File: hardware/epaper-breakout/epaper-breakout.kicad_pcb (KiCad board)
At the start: 2 copper layers, 100 x 40.5 mm, 88 parts, among them J1 XF2M-3315-1A, J2 C10418, J3 Conn_02x06_Counter_Clockwise, J4 ED060SC4, J5 Conn_01x02_Male, Q1 AO3401A, Q2 AO3401A, Q3 MMBT3904, Q4 MMBT3904, Q5 AO3401A, Q6 MMBT3904, U1 MCP1700-3302E_SOT23, U10 ED060SC7, U11 TP4056, U12 CH340C, U2 LT1945, U3 LT1945, U4 XC6206PxxxMR, U5 ESP32-WROVER, U6 ED060XC5, U7 LM358, U8 74HC4094-normal, U9 MCP9700AT-ETT

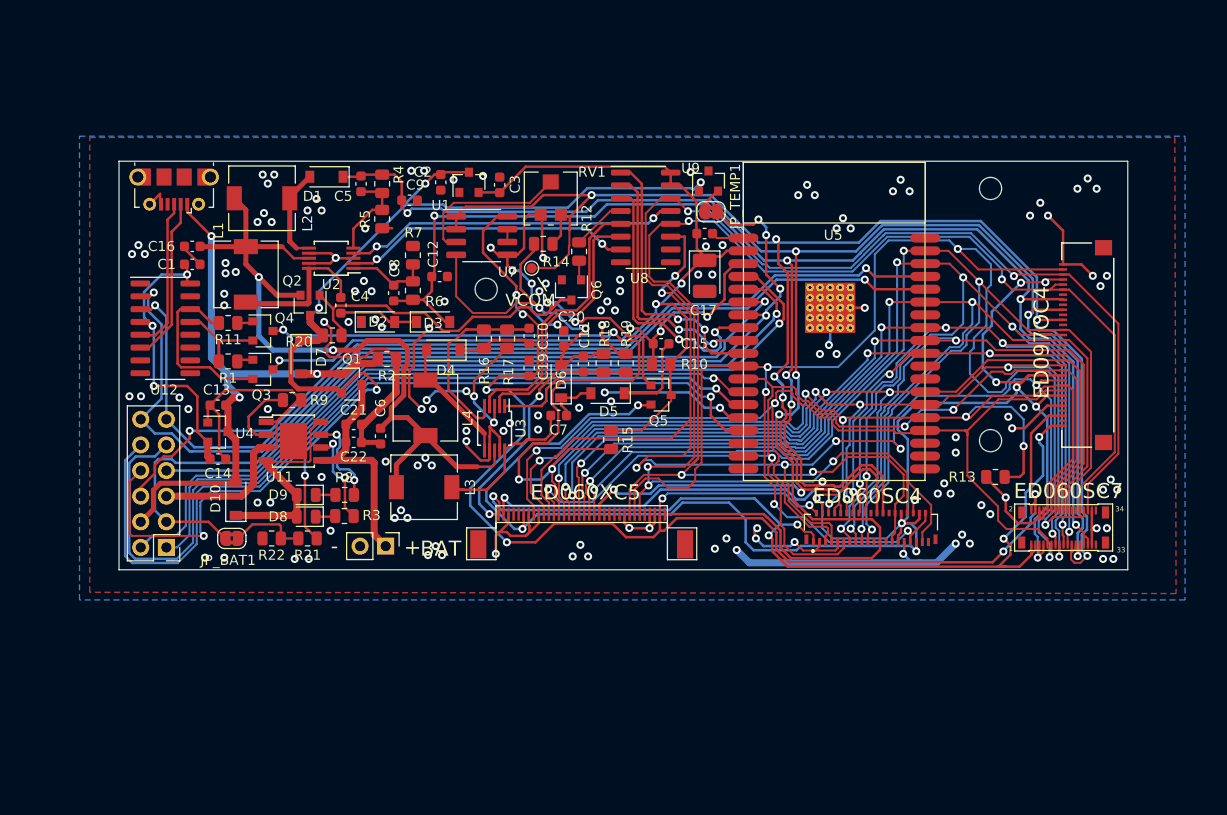
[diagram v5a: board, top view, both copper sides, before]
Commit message: add decoupling cap to battery voltage sensor
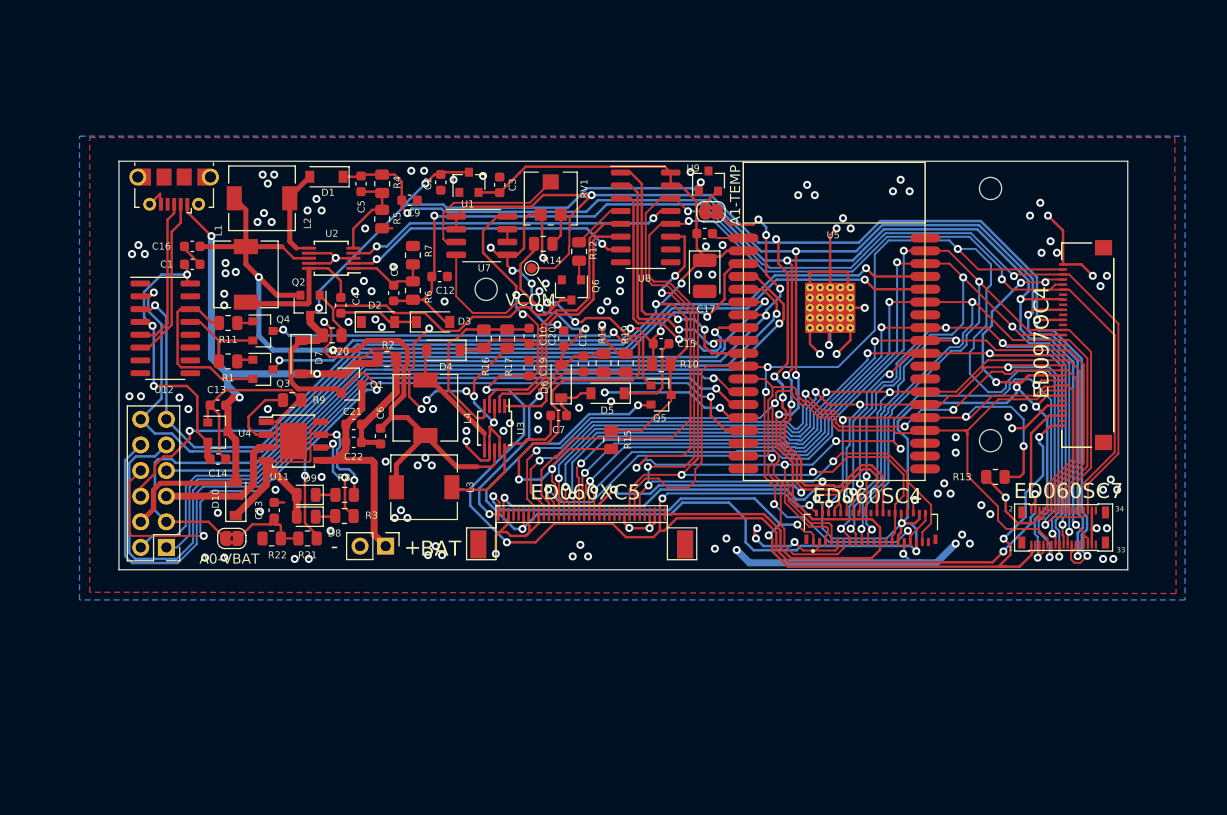
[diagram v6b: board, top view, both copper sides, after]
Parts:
- added C23: 0.1uF, Capacitor_SMD:C_0603_1608Metric, F.Cu at (40.4, 54.1)
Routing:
- net GND: track 257.4 -> 286.4 mm, vias 147 -> 148
- net Net-(C23-Pad2): track 7.83 -> 10.0 mm
- net Net-(D10-Pad1): track 21.9 -> 22.5 mm
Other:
- board text added: "A0-VBAT"
- board text added: "A1-TEMP"
- board text added: "epdiy v5 by Valentin Roland 2021 Thanks to the epdiy contributors!"
- board text removed: "EPaper Breakout v5 by Valentin Roland 2021"

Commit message: v5: swap gpio 0 and 19
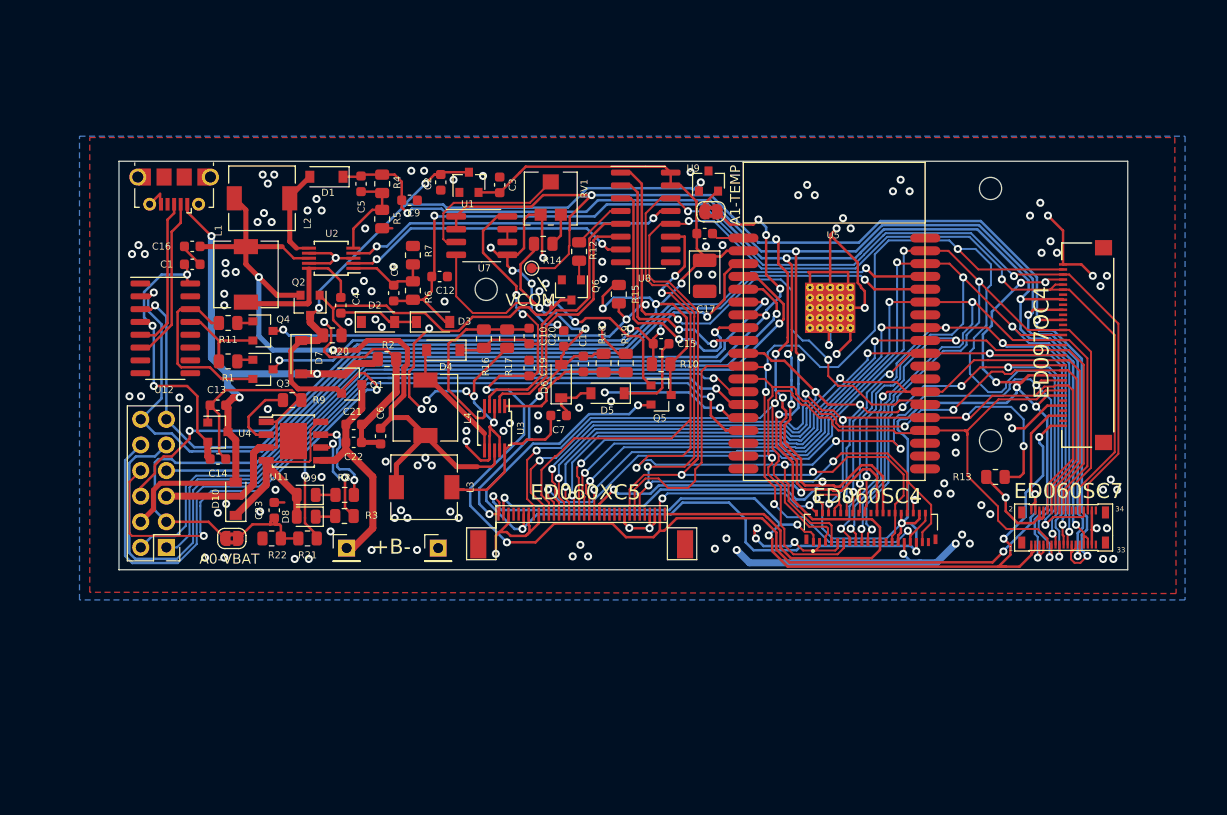
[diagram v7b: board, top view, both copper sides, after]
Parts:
- added J6: Conn_01x01_Male, Connector_PinHeader_2.54mm:PinHeader_1x01_P2.54mm_Vertical, F.Cu at (56.6, 57.8)
- J5: value Conn_01x02_Male -> Conn_01x01_Male; footprint Connector_PinHeader_2.54mm:PinHeader_1x02_P2.54mm_Vertical -> Connector_PinHeader_2.54mm:PinHeader_1x01_P2.54mm_Vertical
- R21: value 800k -> 680k
- R22: value 200k -> 150k
- moved R15 14.5 mm to (74.5, 32.7)
- moved J5 3.88 mm to (47.6, 57.8), turned to 0 degrees
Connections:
- Q4 pad 3: /EP_D0 -> /IO0
- R15 pad 2: /EP_D0 -> /IO0
- U5 pad 10: Net-(U5-Pad10) -> /EP_D0
- U5 pad 25: /EP_D0 -> /IO0
- U8 pad 1: Net-(U5-Pad10) -> /IO0
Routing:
- net /IO0: track 0.00 -> 95.1 mm, vias 0 -> 5
- net /EP_D0: track 168.2 -> 105.9 mm, vias 9 -> 8
- net Net-(U5-Pad10): track 27.9 -> 0.00 mm, vias 2 -> 0
- net GND: track 286.4 -> 292.1 mm, vias 148 -> 147
- net /EP_D1: track 95.2 -> 100.0 mm
- net /EP_CKV: track 147.8 -> 150.4 mm
- net /+3.3V: track 122.6 -> 124.1 mm, vias 3 -> 4
- net /EP_VCOM: track 178.2 -> 176.9 mm
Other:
- board text added: "+B-"
- board text removed: "+"
- board text removed: "-"
- board text removed: "BAT"

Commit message: v5 prototype
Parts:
- moved U9 33.4 mm to (116.6, 24.6), turned to 180 degrees
- moved JP_TEMP1 28.9 mm to (112.4, 27.4), turned to 180 degrees
- moved R2 23.0 mm to (36.4, 21.8), turned to 270 degrees
- moved D4 8.57 mm to (57.0, 46.8)
- moved L2 4.14 mm to (43.3, 23.4)
- moved C10 3.38 mm to (65.3, 40.2), turned to 90 degrees
- moved D1 3.37 mm to (48.6, 22.4), turned to 270 degrees
- moved C19 3.06 mm to (65.3, 37.0)
- moved L4 3.06 mm to (55.7, 40.9), turned to 90 degrees
- moved R17 3.00 mm to (61.0, 38.9), turned to 90 degrees
- moved R16 2.80 mm to (63.3, 38.9), turned to 270 degrees
- moved C9 2.05 mm to (54.9, 25.1), turned to 90 degrees
- moved C5 1.73 mm to (50.7, 21.5)
- moved R4 1.73 mm to (52.8, 21.5)
- moved R5 1.73 mm to (52.8, 25.0)
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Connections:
- U9 pad 1: VIN -> EPD_VDD
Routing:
- net VIN: track 93.4 -> 61.8 mm, vias 5 -> 4
- net GND: track 292.1 -> 261.5 mm, vias 147 -> 132
- net /A1: track 83.9 -> 100.9 mm, vias 4 -> 2
- net /15V: track 149.4 -> 139.3 mm
- net Net-(C10-Pad1): track 19.1 -> 9.26 mm
- net EPD_VDD: track 174.3 -> 181.5 mm, vias 11 -> 12
- net Net-(JP_TEMP1-Pad1): track 2.64 -> 7.06 mm
- net /+3.3V: track 124.1 -> 128.3 mm
- net Net-(C11-Pad1): track 14.1 -> 16.1 mm
- net SW_VIN: track 76.0 -> 77.5 mm
- net /EP_STV: track 151.3 -> 152.7 mm
- net VBUS: track 60.4 -> 61.6 mm
- net /EP_MODE: track 141.9 -> 140.8 mm
- net BAT+: track 22.4 -> 21.3 mm
- net Net-(D4-Pad2): track 12.7 -> 11.9 mm
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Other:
- outline, holes or cut-outs redrawn
